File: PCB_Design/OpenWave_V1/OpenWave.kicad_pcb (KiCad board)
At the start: 4 copper layers, 90 x 60 mm, 110 parts, among them J1 Conn_01x04_Pin, J2 Micro_SD_Card_Det1, J3 SJ1-3545N, J4 USB_C_Receptacle_USB2.0_16P, J5 Conn_01x02_Pin, SW3 SW_Push, SW4 SW_Push, SW5 SW_Push, SW6 SW_Push, SW8 SW_SPDT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

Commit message: Completed PCB Design, Updated Licences and Readme.
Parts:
- added C23: 0.1uF, Capacitor_SMD:C_0603_1608Metric, F.Cu at (103.0, 106.0)
- added C24: 0.1uF, Capacitor_SMD:C_0603_1608Metric, F.Cu at (106.5, 123.2)
- added C47: 470uF, Capacitor_THT:CP_Radial_D5.0mm_P2.00mm, F.Cu at (110.7, 114.9)
- added R22: 10K, Resistor_SMD:R_0603_1608Metric, F.Cu at (101.4, 106.0)
- added R23: 10K, Resistor_SMD:R_0603_1608Metric, F.Cu at (106.5, 124.8)
- added SW1: SW_Push, GlobalFP:TS3315A, F.Cu at (96.0, 112.2)
- added SW2: SW_Push, GlobalFP:TS3315A, F.Cu at (96.0, 126.8)
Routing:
- net /BOOT: track 0.00 -> 44.4 mm, vias 0 -> 2
- net /EN: track 0.00 -> 42.6 mm, vias 0 -> 2
- net GND: track 84.8 -> 89.3 mm, vias 74 -> 80
- net +3V3: track 33.3 -> 31.6 mm, vias 35 -> 48
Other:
- board text added: "OpenWave"

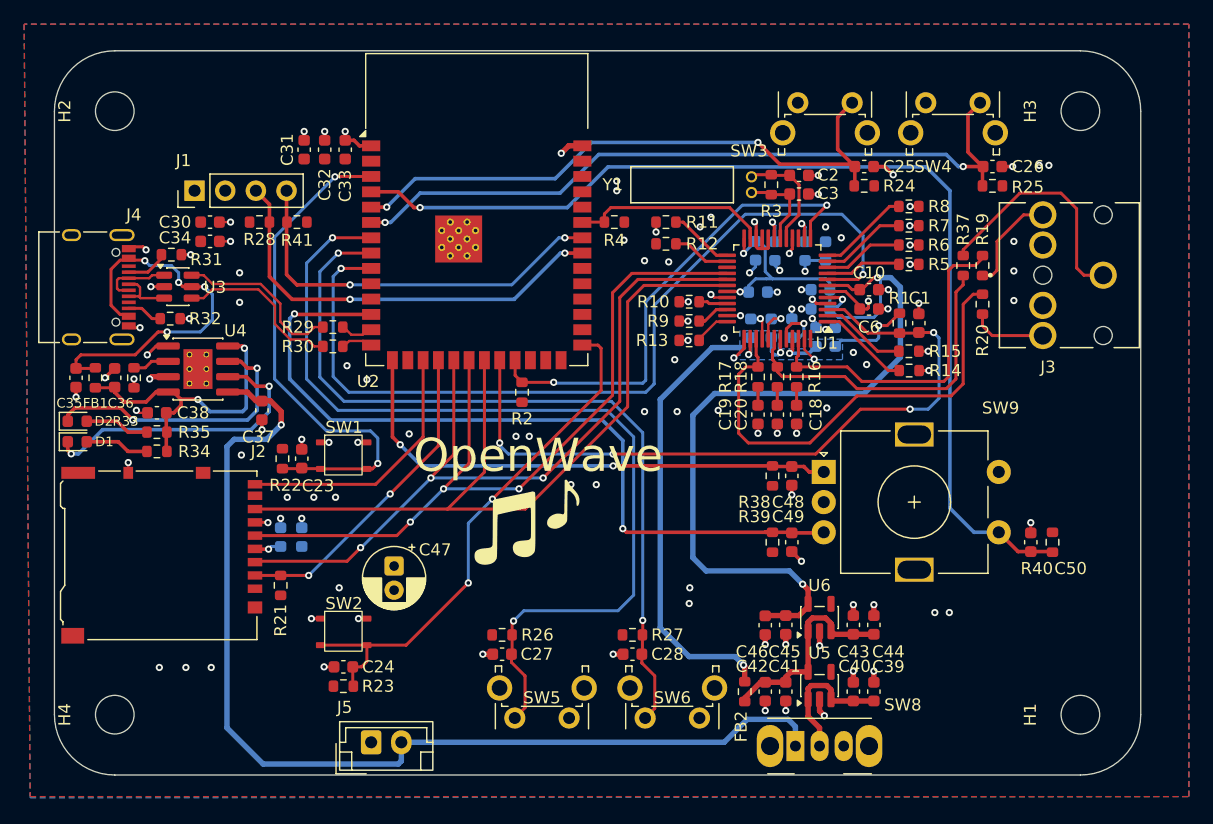
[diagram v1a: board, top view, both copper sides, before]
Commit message: Added power indicators and silkscreen
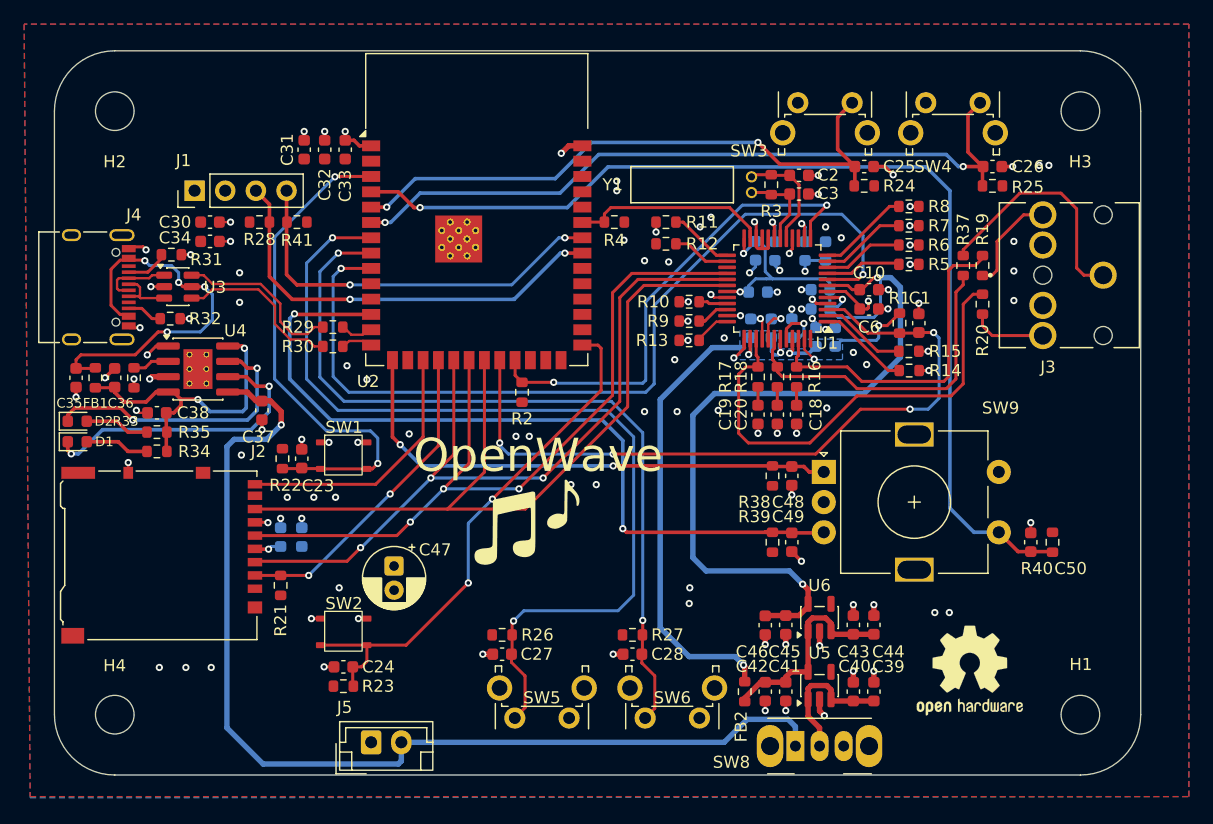
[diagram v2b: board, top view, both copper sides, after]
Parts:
- added REF**: OSHW-Logo2_9.8x8mm_SilkScreen, Symbol:OSHW-Logo2_9.8x8mm_SilkScreen, F.Cu at (158.3, 123.5)

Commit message: Minor tracing updates
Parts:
- added D3: LED, LED_SMD:LED_0603_1608Metric, F.Cu at (152.2, 119.8)
- added D4: LED, LED_SMD:LED_0603_1608Metric, F.Cu at (139.8, 119.8)
- added R36: 330E, Resistor_SMD:R_0603_1608Metric, F.Cu at (153.8, 119.8)
- added R42: 330E, Resistor_SMD:R_0603_1608Metric, F.Cu at (138.1, 119.9)
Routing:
- net +3V3: track 31.6 -> 36.0 mm, vias 48 -> 50
- net Net-(D3-K): track 0.00 -> 1.74 mm
- net Net-(D4-K): track 0.00 -> 1.68 mm
- net +1V8: track 88.0 -> 89.6 mm
- net GND: track 89.3 -> 90.7 mm, vias 80 -> 83

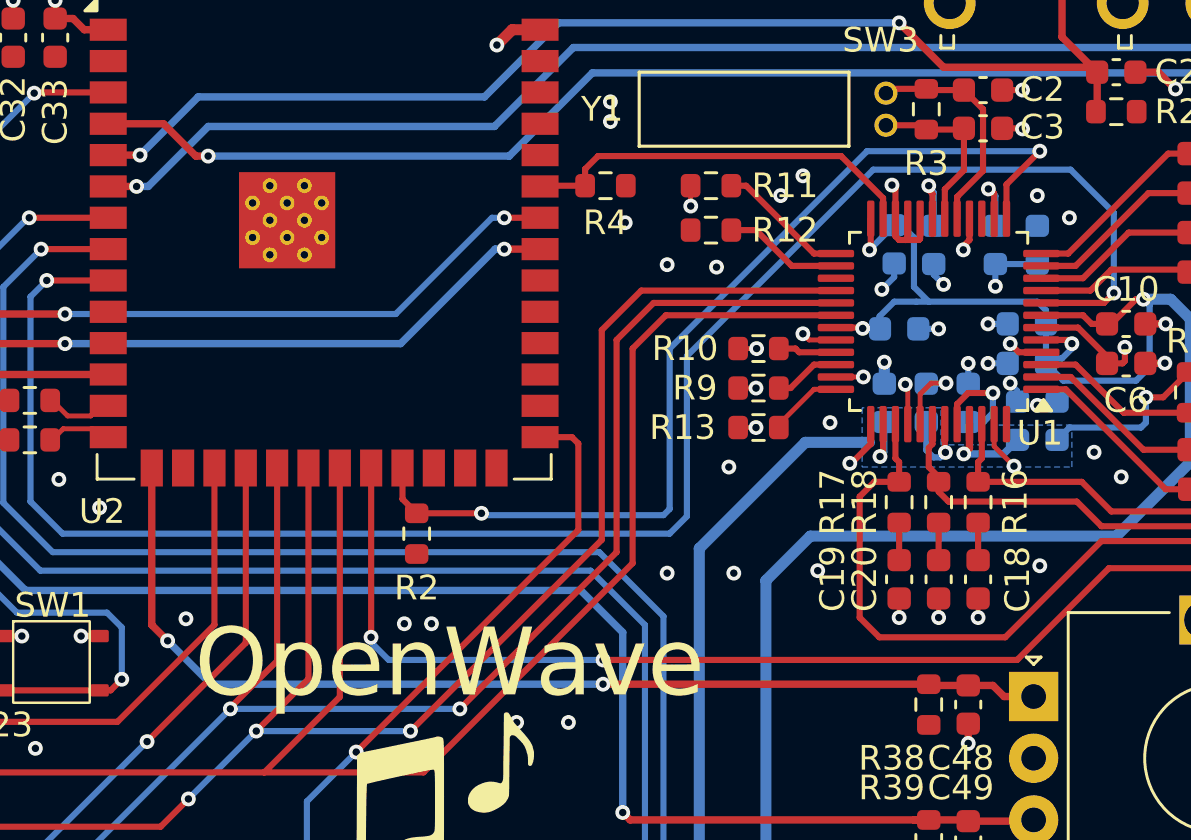
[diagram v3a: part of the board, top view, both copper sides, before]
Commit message: Updated BOM,  Changed ESP pin defs.
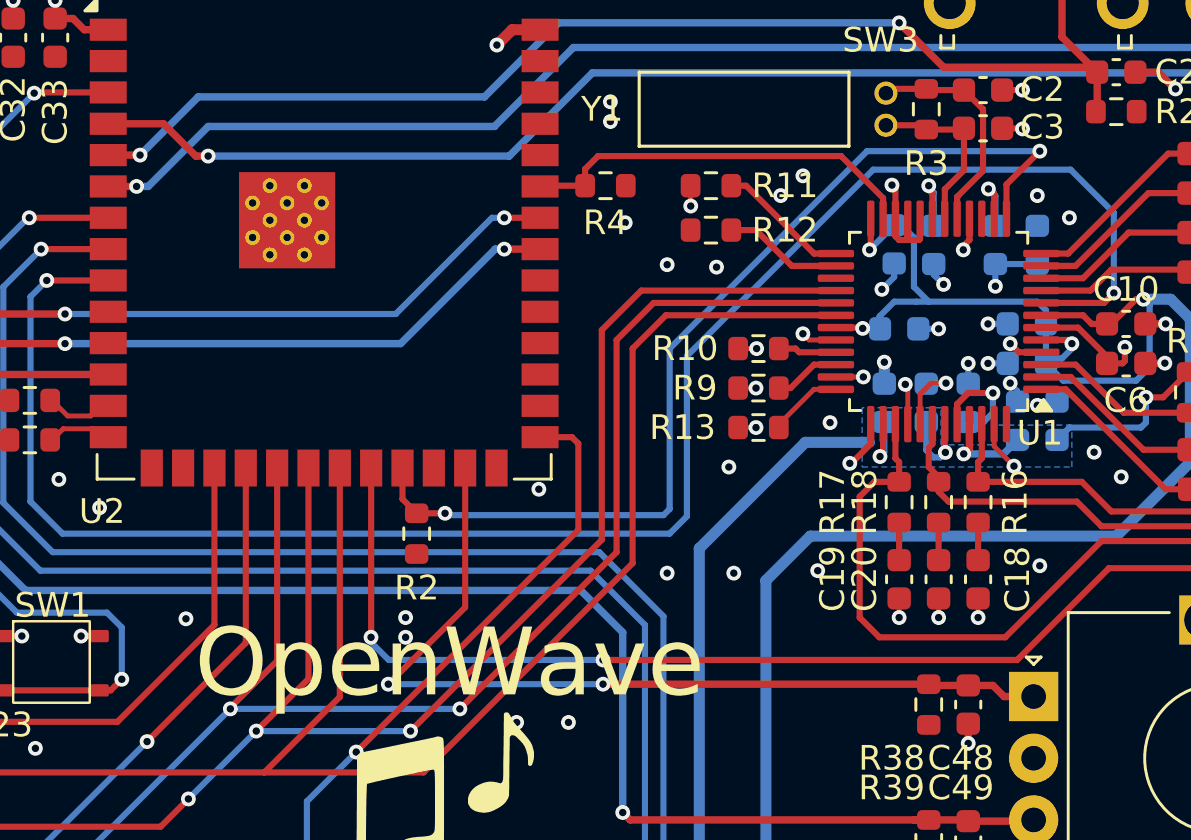
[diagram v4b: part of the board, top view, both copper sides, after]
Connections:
- U2 pad 15: /Rotary1 -> unconnected-(U2-IO3-Pad15)
- U2 pad 25: unconnected-(U2-IO48-Pad25) -> /Rotary1
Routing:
- net /Rotary1: track 43.3 -> 36.4 mm
- net +3V3: vias 50 -> 51

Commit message: Update README
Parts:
- moved C10 0.20 mm to (150.0, 92.2)
- moved C11 0.20 mm to (140.8, 92.4)
- moved C12 0.20 mm to (146.0, 93.8)
- moved C14 0.20 mm to (145.6, 96.1)
- moved C15 0.20 mm to (140.2, 95.4)
- moved C16 0.20 mm to (147.2, 96.1)
- moved C17 0.20 mm to (141.9, 95.4)
- moved C18 0.20 mm to (144.0, 102.5)
- moved C19 0.20 mm to (140.8, 102.5)
- moved C20 0.20 mm to (142.4, 102.5)
- moved C21 0.20 mm to (101.2, 112.7)
- moved C22 0.20 mm to (103.0, 112.7)
- moved C23 0.20 mm to (103.0, 106.2)
- moved C24 0.20 mm to (106.5, 123.5)
- moved C25 0.20 mm to (149.6, 82.0)
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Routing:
- net +3V3: vias 51 -> 48
